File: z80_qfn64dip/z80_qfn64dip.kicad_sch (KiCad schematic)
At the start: 58 parts, among them J1 Conn_08, U1 Caravel_QFN, U2 Z80CPU, U3 TPS7A2018PDQNRM3, U4 TPS7A2033PDQNRM3, U5 TPS7A2050PDQNRM3, U6 AT25EU0081A, X1 10MHz

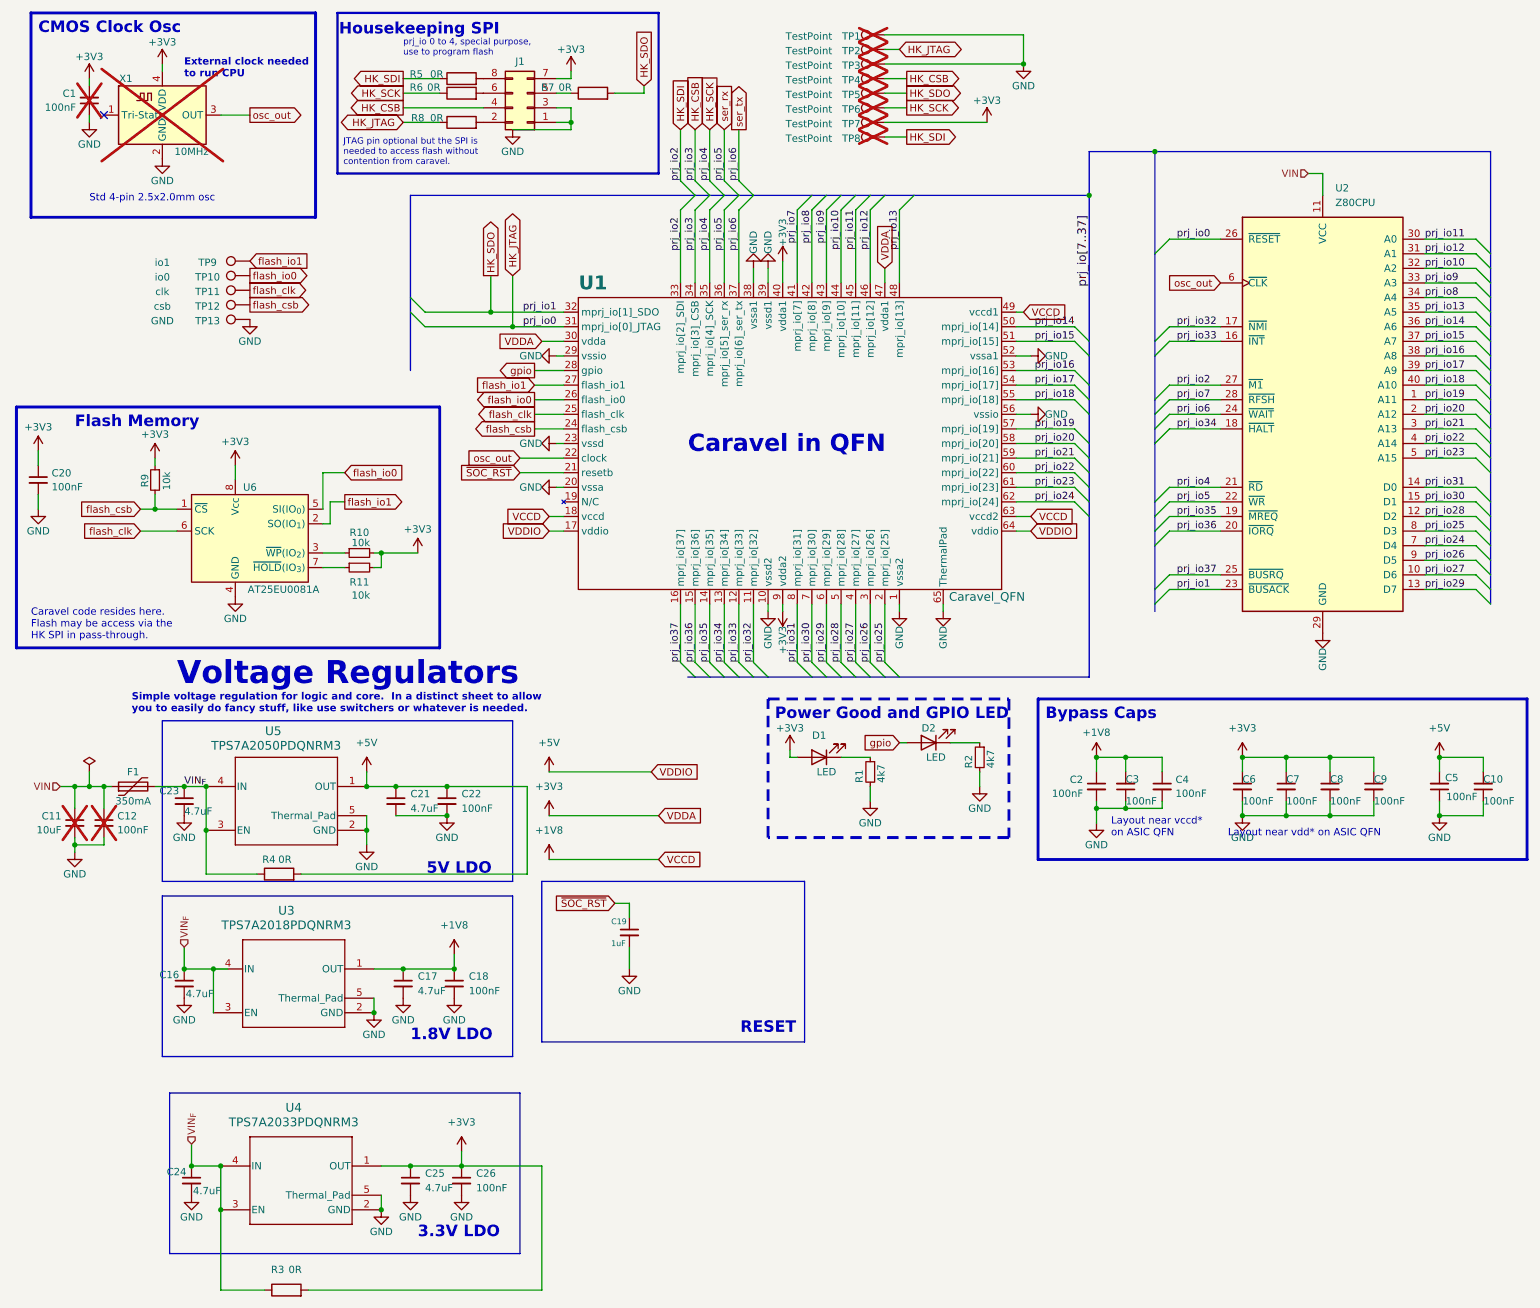
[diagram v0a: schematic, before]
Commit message: minor layout position tweaks; move schematics around a bit; add aisler user design rule
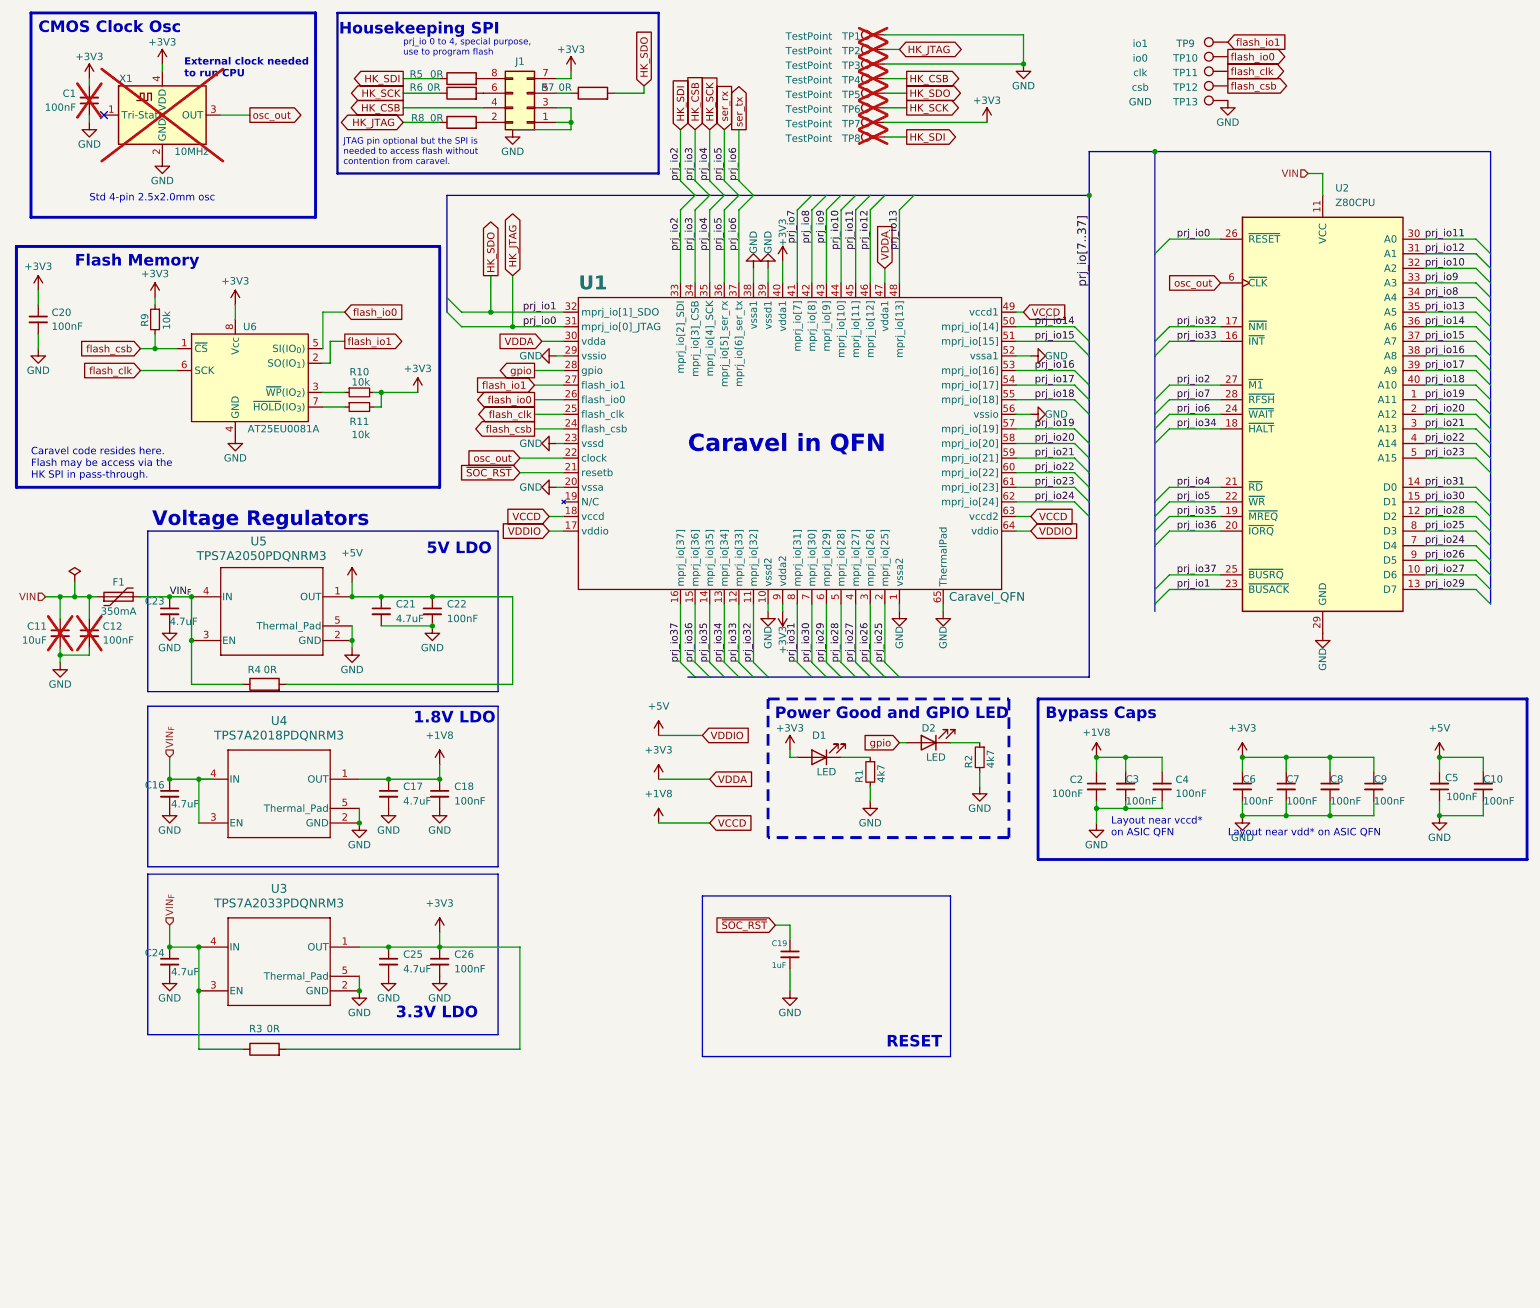
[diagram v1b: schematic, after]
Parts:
- renumbered U4 to U3, U3 to U4
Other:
- note removed: "Simple voltage regulation for logic and core. In a distinct sheet to allow you to easily do fancy stuff, like use switchers or whatever is needed."
- moved on the sheet: C11, C12, C16, C17, C18, C19, C20, C21, C22, C23, C24, C25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
